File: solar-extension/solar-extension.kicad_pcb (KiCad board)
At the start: 2 copper layers, 21.5 x 36 mm, 2 parts, among them J1 302-S201, J2 M55-6021242R

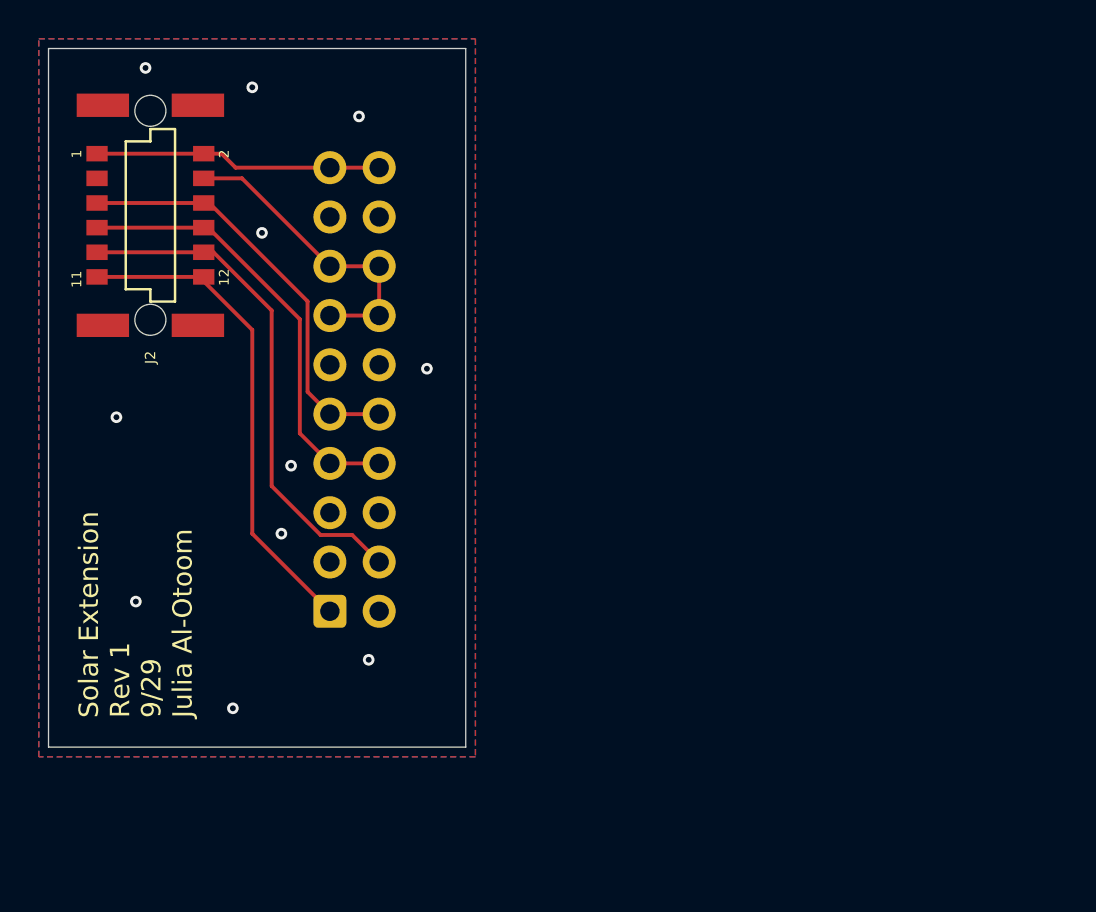
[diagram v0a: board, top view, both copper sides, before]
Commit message: final changes made to sizing after design review
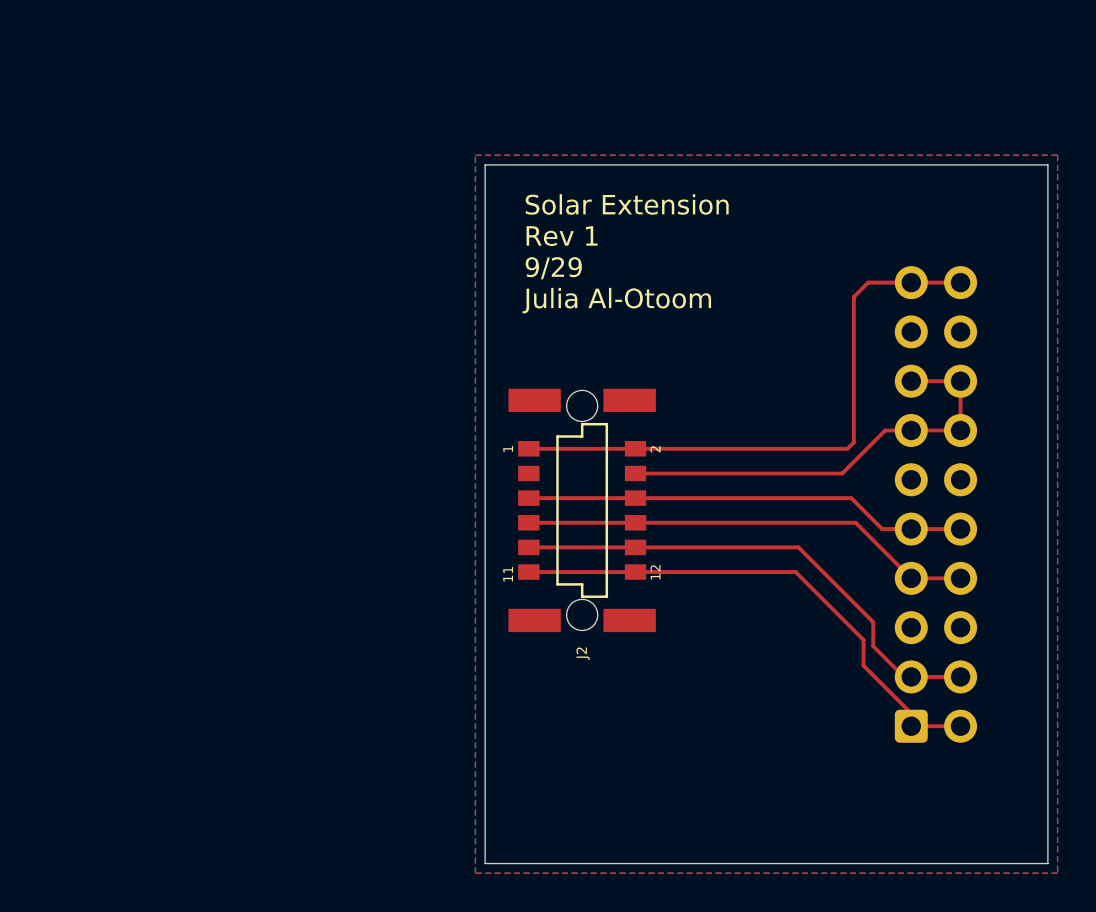
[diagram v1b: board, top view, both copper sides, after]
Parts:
- moved J1 30.5 mm to (254.0, 77.4)
- moved J2 27.0 mm to (237.0, 66.3)
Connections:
- J1 pad 2: GND -> /SM-UART-RX
- J1 pad 3: GND -> /SM-UART-TX
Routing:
- net /~{SD}: track 14.8 -> 30.2 mm
- net /VBUS: track 16.0 -> 22.7 mm
- net /SM-UART-RX: track 25.4 -> 26.7 mm
- net /CAN_H: track 21.8 -> 22.9 mm
- net /SM-UART-TX: track 26.5 -> 25.7 mm
- net GND: vias 11 -> 0
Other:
- board size 21.5 x 36 mm -> 29 x 36 mm

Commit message: final final changes made to pinout, track width, and added vias
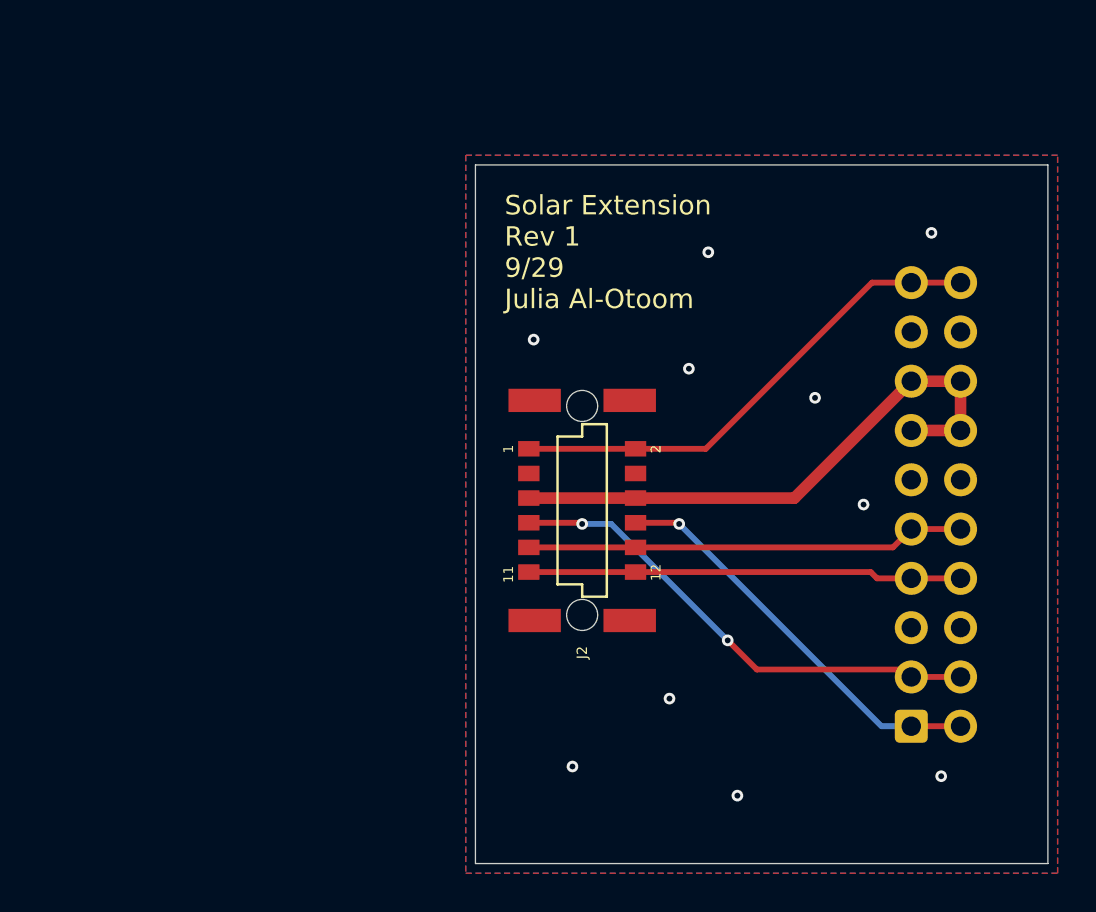
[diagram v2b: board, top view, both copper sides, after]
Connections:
- J2 pad 10: /SM-UART-TX -> /CAN_H
- J2 pad 11: /SM-UART-RX -> /CAN_L
- J2 pad 12: /SM-UART-RX -> /CAN_L
- J2 pad 4: /VBUS -> GND
- J2 pad 5: /CAN_H -> /VBUS
- J2 pad 6: /CAN_H -> /VBUS
- J2 pad 7: /CAN_L -> /SM-UART-TX
- J2 pad 8: /CAN_L -> /SM-UART-RX
- J2 pad 9: /SM-UART-TX -> /CAN_H
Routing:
- net /VBUS: track 22.7 -> 29.8 mm
- net /SM-UART-RX: track 26.7 -> 21.1 mm, vias 0 -> 1
- net /~{SD}: track 30.2 -> 25.8 mm
- net /CAN_L: track 23.4 -> 22.4 mm
- net /SM-UART-TX: track 25.7 -> 25.5 mm, vias 0 -> 2
- net GND: vias 0 -> 10
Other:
- board size 29 x 36 mm -> 29.5 x 36 mm

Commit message: minor polishing and imported 2 layer OSH Park design rules.
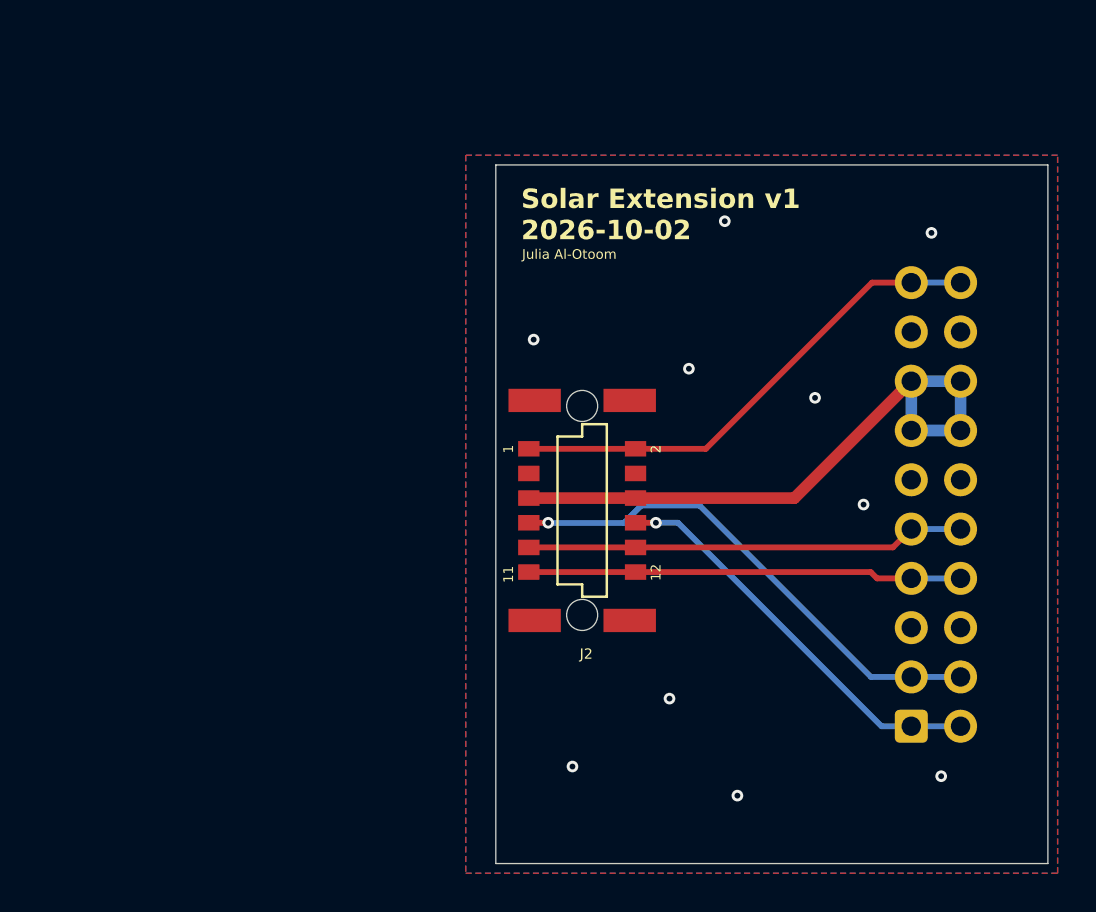
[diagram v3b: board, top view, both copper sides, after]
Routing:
- net /VBUS: track 29.8 -> 32.4 mm
- net /SM-UART-TX: track 25.5 -> 26.3 mm, vias 2 -> 1
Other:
- board size 29.5 x 36 mm -> 28.4 x 36 mm
- board text added: "${TITLE} v${REVISION} ${ISSUE_DATE}"
- board text added: "Julia Al-Otoom"
- board text removed: "Solar Extension Rev 1 9/29 Julia Al-Otoom"
